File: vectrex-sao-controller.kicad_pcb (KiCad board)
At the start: 2 copper layers, 38.5 x 18.6 mm, 2 parts

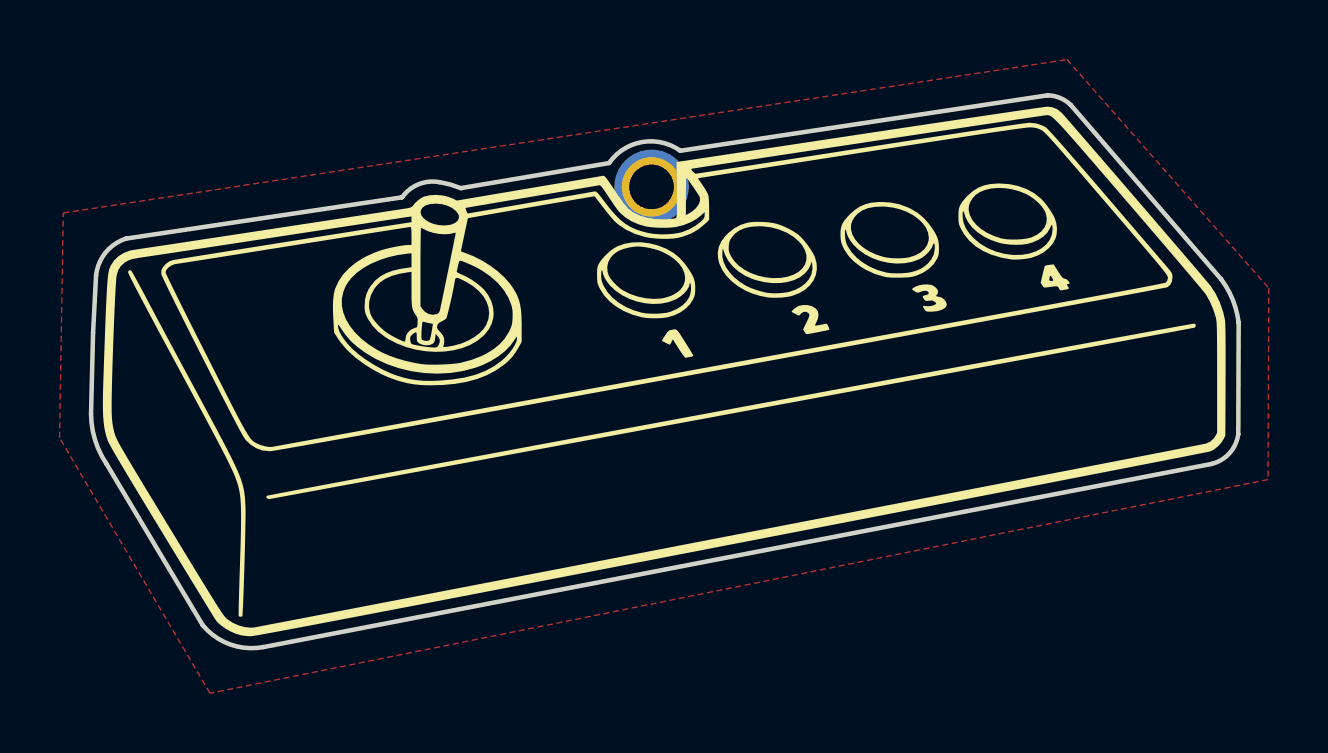
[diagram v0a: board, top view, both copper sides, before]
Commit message: updated models and created files for ordering
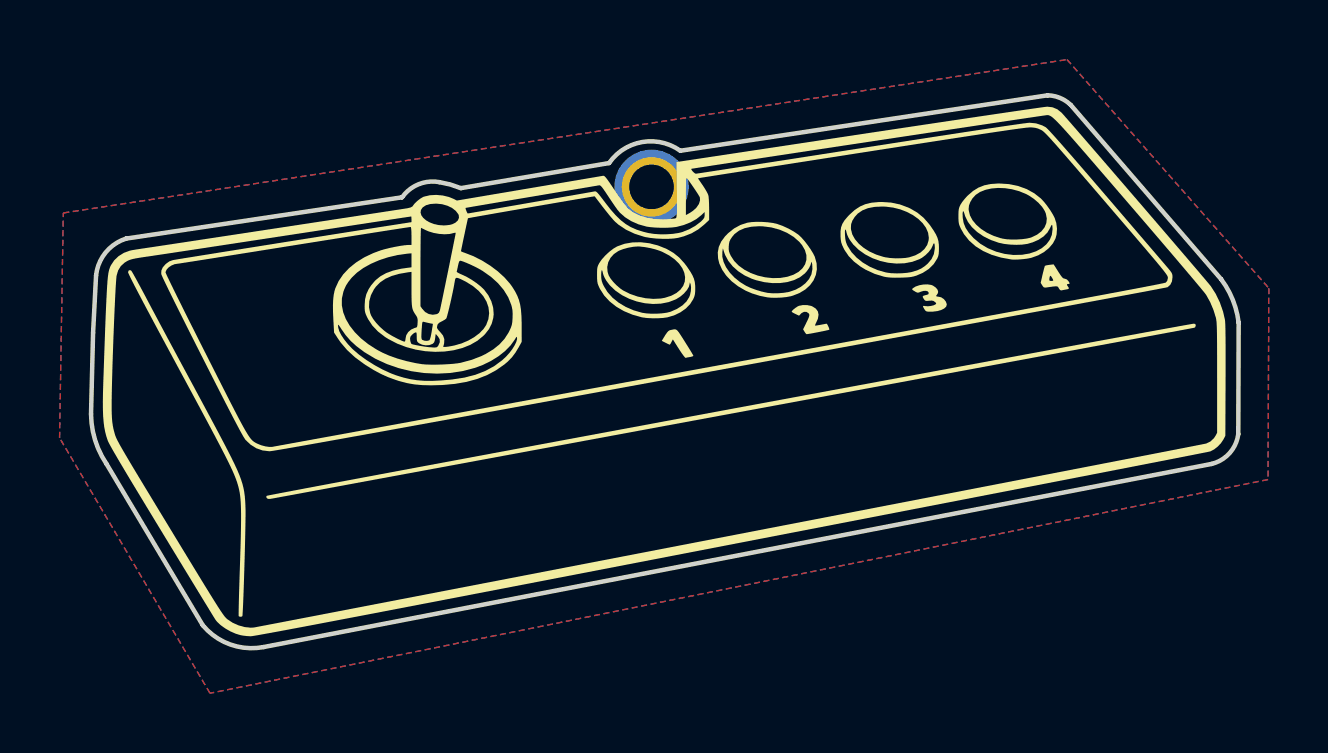
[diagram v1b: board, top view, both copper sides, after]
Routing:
- added copper zone on B.Cu, net /TOUCH_PAD
- added copper zone on F.Cu, net /TOUCH_PAD
- removed copper zone on F.Cu, net (none)
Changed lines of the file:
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@@
       (layerselection 0x00010fc_ffffffff)
       (disableapertmacros false)
-      (usegerberextensions false)
+      (usegerberextensions true)
       (usegerberattributes true)
       (usegerberadvancedattributes true)
-      (creategerberjobfile true)
+      (creategerberjobfile false)
       (svguseinch false)
       (svgprecision 6)
@@
       (outputformat 1)
       (mirror false)
-      (drillshape 1)
+      (drillshape 0)
       (scaleselection 1)
-      (outputdirectory "")
+      (outputdirectory "gerbers/")
     )
   )
@@
     (property "Sheetname" "")
     (attr exclude_from_pos_files)
-    (fp_text reference "JP1" (at 0 3.2) (layer "B.SilkS")
+    (fp_text reference "JP1" (at 0 3.2) (layer "B.SilkS") hide
       (effects (font (size 1 1) (thickness 0.15)) (justify mirror))
     )
-    (fp_text value "TOUCH_PAD" (at 0 -3.2) (layer "B.Fab")
+    (fp_text value "TOUCH_PAD" (at 0 -3.2) (layer "B.Fab") hide
       (effects (font (size 1 1) (thickness 0.15)) (justify mirror))
     )
-    (fp_text user "${REFERENCE}" (at 0 0) (layer "B.Fab")
+    (fp_text user "${REFERENCE}" (at 0 0) (layer "B.Fab") hide
       (effects (font (size 1 1) (thickness 0.15)) (justify mirror))
     )
@@
   (gr_line (start 139.962761 91.833229) (end 139.95 95.575) (layer "Edge.Cuts") (width 0.15))
   (gr_line (start 134.326135 84.524588) (end 139.375 90.375) (layer "Edge.Cuts") (width 0.15))
-  (zone (net 0) (net_name "") (layer "F.Cu") (hatch edge 0.508)
+  (zone (net 1) (net_name "/TOUCH_PAD") (layer "F.Cu") (hatch edge 0.508)
     (connect_pads (clearance 0.508))
     (min_thickness 0.254) (filled_areas_thickness no)
@@
         (xy 140.975 90.675)
         (xy 140.95 97.1)
+        (xy 105.425 104.275)
+        (xy 100.375 95.7)
+        (xy 100.5 88.15)
+        (xy 134.2 83)
+      )
+    )
+  )
+  (zone (net 1) (net_name "/TOUCH_PAD") (layer "B.Cu") (hatch edge 0.508)
+    (connect_pads (clearance 0.508))
+    (min_thickness 0.254) (filled_areas_thickness no)
+    (fill yes (thermal_gap 0.508) (thermal_bridge_width 0.508))
+    (polygon
+      (pts
+        (xy 140.975 90.675)
         (xy 140.95 97.1)
         (xy 105.425 104.275)
